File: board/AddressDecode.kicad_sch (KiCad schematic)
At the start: 24 parts, among them U10 74LS260, U11 74F86, U12 74F20, U13 74F30, U14 74F32, U15 74F00, U16 74LS154, U17 74F541, U18 74F138, U19 74F240, U8 74LS260, U9 74F08

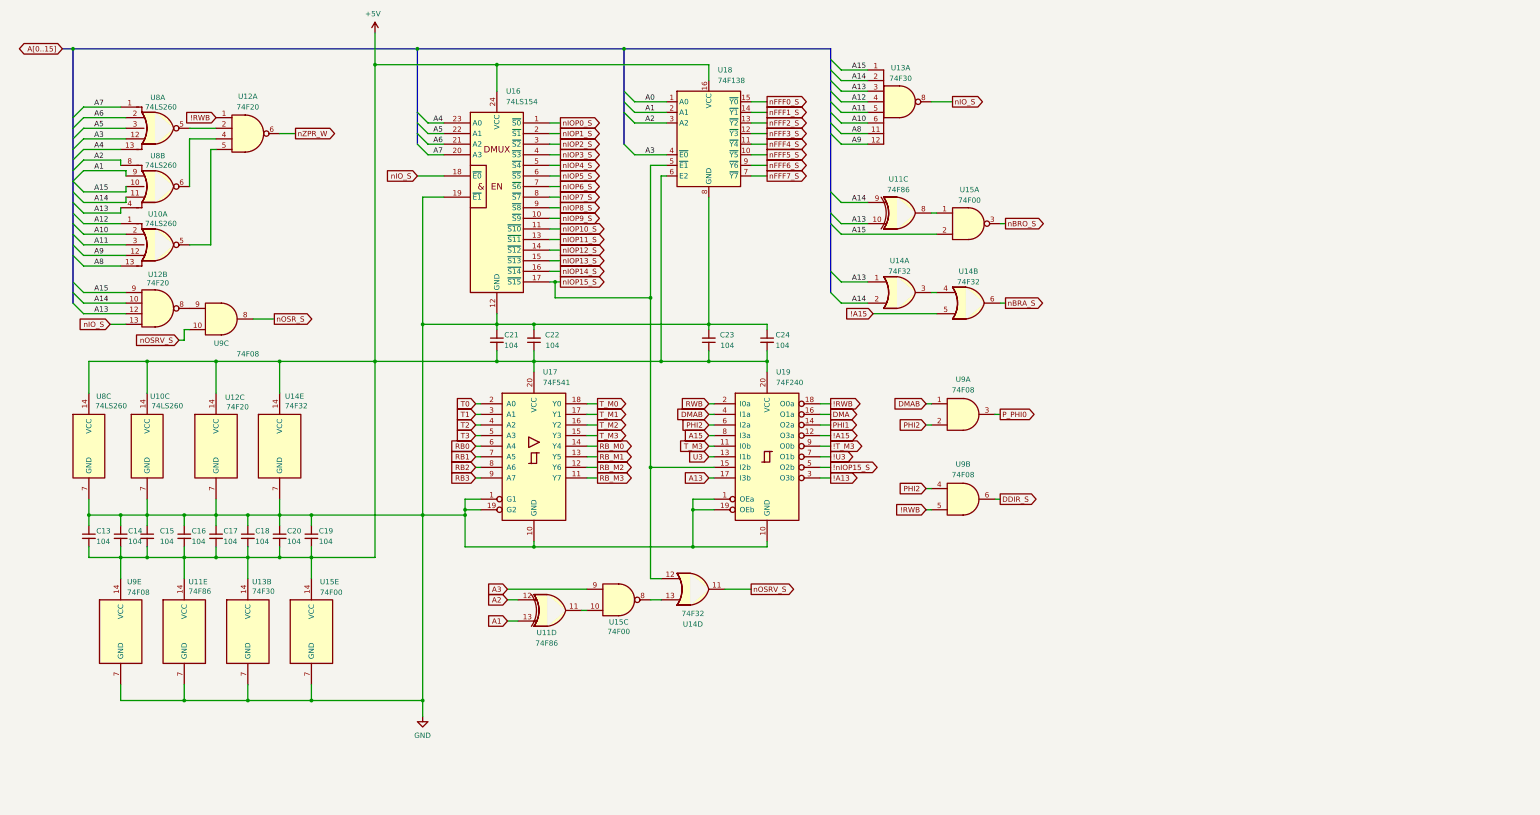
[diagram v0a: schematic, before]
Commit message: V2.0: wait states, GAL glue logic, serial clock and review fixes
Main board schematic:
- Replace the T4-T7 clock divider with RDY wait states. Fixed 7.16 MHz
  CPU clock; J36 selects 3.58 MHz for Rockwell parts. Waits are set per
  region through the write-only register at $FFF5 (reset = 3 waits).
- Move address decode, strobes, the wait-state generator, the IRQ
  encoder/latch/vector mux, ROM bank gating and DMA sync into seven GALs
  (U81-U86 ATF22V10C, U87 ATF16V8C), removing 29 ICs. CUPL sources,
  JEDECs and notes are in board/PLDs/V2.
- 1.8432 MHz serial clock, soft-power latch, -5V regulator, bulk caps,
  pull-ups, audio coupling/decoupling, GNDA tie, read-only Z register
  and other design-review fixes.
- New WaitStates and Support sheets; project symbol library
  hydra16.kicad_sym with sym-lib-table.

PCB updated from the schematic. Includes pending changes to the counter,
bus breakout and memory daughter card projects.

Firmware:
- Remove S_REGISTER; T/U/V/W now at $FFF0-$FFF3 to match the hardware.
- Add math.s and sound.s (included by os_main.s).
- Rebuild the 65C02 ROM image.

Co-Authored-By: Claude Opus 5.5 <noreply@anthropic.com>
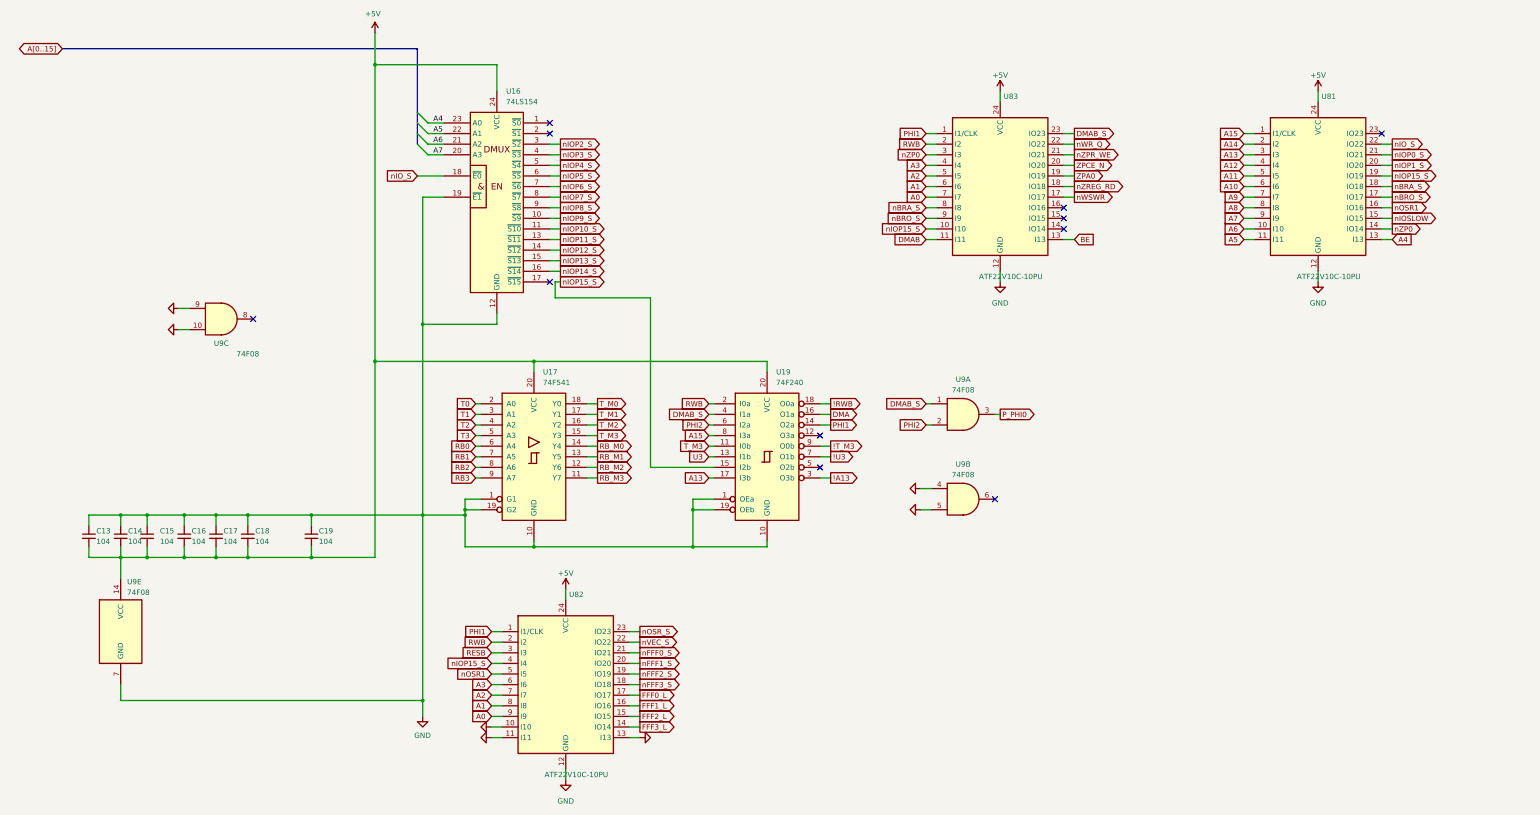
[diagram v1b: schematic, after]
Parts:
- removed C20, C21, C22, C23, C24: 104, Capacitor_THT:C_Disc_D5.0mm_W2.5mm_P5.00mm, symbol Device:C_Small
- removed U10, U8: 74LS260, Package_DIP:DIP-14_W7.62mm_Socket_LongPads, symbol Other_TTL:74LS260
- removed U11: 74F86, Package_DIP:DIP-14_W7.62mm_Socket_LongPads, symbol 74xx:74LS86
- removed U12: 74F20, Package_DIP:DIP-14_W7.62mm_Socket_LongPads, symbol 74xx:74LS20
- removed U13: 74F30, Package_DIP:DIP-14_W7.62mm_Socket_LongPads, symbol 74xx:74LS30
- removed U14: 74F32, Package_DIP:DIP-14_W7.62mm_Socket_LongPads, symbol 74xx:74LS32
- removed U15: 74F00, Package_DIP:DIP-14_W7.62mm_Socket_LongPads, symbol 74xx:74LS00
- removed U18: 74F138, Package_DIP:DIP-16_W7.62mm_Socket_LongPads, symbol 74xx:74HC138
- added U81, U82, U83: ATF22V10C-10PU, Package_DIP:DIP-24_W7.62mm_Socket_LongPads, symbol Hydra16:ATF22V10C
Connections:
- net nOSRV_S is gone; now on net GND: U9.10
- net !RWB: no longer U9.5
- net +5V: now also U81.24 (VCC), U82.24 (VCC), U83.24 (VCC)
- net A0: now also U82.9 (I9), U83.7 (I7)
- net A1: now also U82.8 (I8), U83.6 (I6)
- net A10: now also U81.6 (I6)
- net A11: now also U81.5 (I5)
- net A12: now also U81.4 (I4)
- net A13: now also U81.3 (I3)
- net A14: now also U81.2 (I2)
- net A15: now also U81.1 (I1/CLK)
- net A2: now also U82.7 (I7), U83.5 (I5)
- net A3: now also U82.6 (I6), U83.4 (I4)
- net A4: now also U81.13 (I13)
- net A5: now also U81.11 (I11)
- net A6: now also U81.10 (I10)
- net A7: now also U81.9 (I9)
- net A8: now also U81.8 (I8)
- net A9: now also U81.7 (I7)
- net DMAB: now also U83.11 (I11); no longer U19.4 (I1a), U9.1
- net GND: now also U9.4, U9.5, U9.9, U81.12 (GND), U82.10 (I10), U82.11 (I11), U82.12 (GND), U82.13 (I13), U83.12 (GND)
- net PHI1: now also U82.1 (I1/CLK), U83.1 (I1/CLK)
- net PHI2: no longer U9.4
- net RWB: now also U82.2 (I2), U83.2 (I2)
- net nBRA_S: now also U81.18 (IO18), U83.8 (I8)
- net nBRO_S: now also U81.17 (IO17), U83.9 (I9)
- net nFFF0_S: now also U82.21 (IO21)
- net nFFF1_S: now also U82.20 (IO20)
- net nFFF2_S: now also U82.19 (IO19)
- net nFFF3_S: now also U82.18 (IO18)
- net nIOP0_S: now also U81.21 (IO21); no longer U16.1 (~{S0})
- net nIOP15_S: now also U81.19 (IO19), U82.4 (I4), U83.10 (I10); no longer U16.17 (~{S15})
- net nIOP1_S: now also U81.20 (IO20); no longer U16.2 (~{S1})
- net nIO_S: now also U81.22 (IO22)
- net nOSR_S: now also U82.23 (IO23); no longer U9.8
- net !A15: no longer names the net of U19.12 (O3a)
- net !nIOP15_S: no longer names the net of U19.5 (O2b)
- net DDIR_S: no longer names the net of U9.6
- new net BE: U83.13 (I13)
- new net DMAB_S: U19.4 (I1a), U83.23 (IO23), U9.1
- new net FFF0_L: U82.17 (IO17)
- new net FFF1_L: U82.16 (IO16)
- new net FFF2_L: U82.15 (IO15)
- new net FFF3_L: U82.14 (IO14)
- new net RESB: U82.3 (I3)
- new net ZPA0: U83.19 (IO19)
- new net ZPCE_N: U83.20 (IO20)
- new net nIOSLOW: U81.15 (IO15)
- new net nOSR1: U81.16 (IO16), U82.5 (I5)
- new net nVEC_S: U82.22 (IO22)
- new net nWR_Q: U83.22 (IO22)
- new net nWSWR: U83.17 (IO17)
- new net nZP0: U81.14 (IO14), U83.3 (I3)
- new net nZPR_WE: U83.21 (IO21)
- new net nZREG_RD: U83.18 (IO18)
- no-connect marks 0 -> 11

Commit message: V2.0 rev 2.0D: clock stretching, OS ROM paging and review fixes
Bus timing:
- New GAL C (U88) generates PHI2/PHI1 and the 3.58 MHz sound clock from
  the 14.318 MHz master, replacing the U35 74F191 divider. J36 now selects
  7.16 or 3.58 MHz.
- Banked RAM, banked ROM and slot I/O ($FF20-$FFEF) get one extra PHI2-low
  period plus 0-3 extra PHI2-high periods set in $FFF5 (GAL D). This
  replaces the on-board RDY wait generator; cards can still pull RDY.
- Write strobes are now hold-time safe: PHI1 comes straight from GAL C
  and RWB_M straight from GAL B2.

Review fixes:
- OS ROM chip enable from a single-level decode, output enable from
  GAL B1; -55 part specified. Full 4K OS ROM paging via GAL G.
- Vector RAM writes only during PHI2; $FFF0-$FFFF no longer slowed.
- YM2151 /WR on RWB_M. U62 removed. RB0-RB7 pull-ups (RN5).
- Slot clocks driven through U56 and U34 with 33R series resistors.
- J38 enables in-system flashing of the banked ROMs.
- W65C22S/W65C51N, AS6C4008, DS1813-5 and CY7C192-25 values; R4 1k.
- J7 pin 8 no longer +5V; +5VA renamed +5VSB; serial handshake loop.
- Sheet titles and revisions, slot symbol pin fixes, and project symbol
  and footprint libraries so the project opens on another machine.

Co-Authored-By: Claude Opus 5.5 <noreply@anthropic.com>
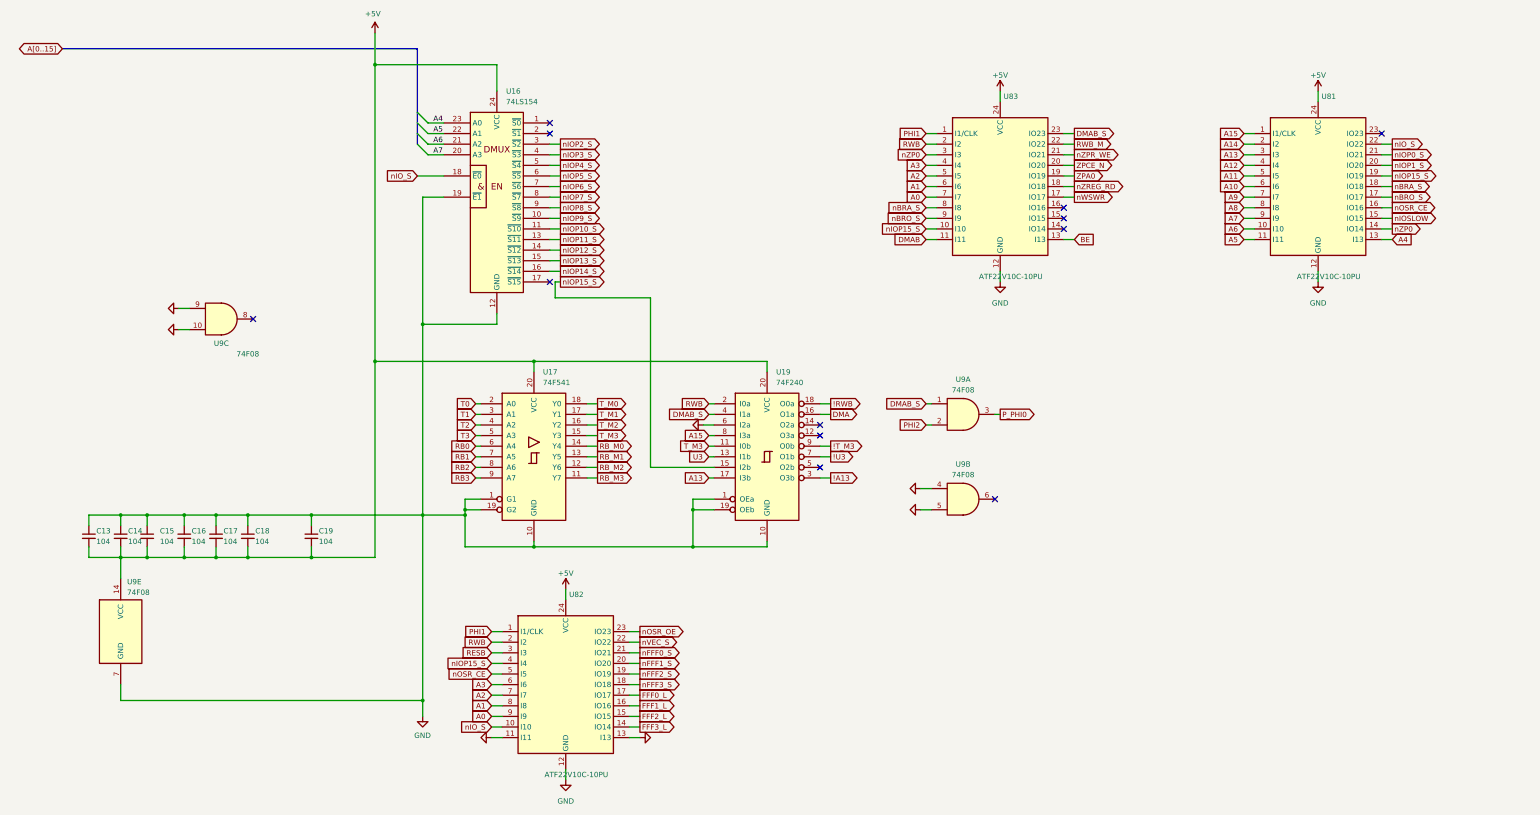
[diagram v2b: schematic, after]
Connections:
- net GND: now also U19.6 (I2a); no longer U82.10 (I10)
- net PHI1: no longer U19.14 (O2a)
- net PHI2: no longer U19.6 (I2a)
- net nIO_S: now also U82.10 (I10)
- net nOSR1 renamed nOSR_CE
- net nOSR_S renamed nOSR_OE
- net nWR_Q renamed RWB_M
- no-connect marks 11 -> 12
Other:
- title: ZeroPage $00/$01 Mirror Memory and RAM/ROM Bank Logic -> Address Decode and Bus Strobes (GALs)
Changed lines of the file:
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@@
 	(paper "USLedger")
 	(title_block
-		(title "ZeroPage $00/$01 Mirror Memory and RAM/ROM Bank Logic")
-		(date "2026-01-28")
-		(rev "2.0B")
+		(title "Address Decode and Bus Strobes (GALs)")
+		(date "2026-10-06")
+		(rev "2.0D")
 		(company "Data Tuning")
 		(comment 1 "Hydra 16")
@@
 		(at 269.24 66.04)
 	)
+	(no_connect
+		(at 210.82 118.11)
+	)
 	(bus_entry
 		(at 114.3 48.26)
@@
 	(wire
 		(pts
-			(xy 134.62 190.5) (xy 132.08 190.5)
-		)
-		(stroke
-			(width 0)
-			(type default)
-		)
-	)
-	(wire
-		(pts
 			(xy 104.14 24.13) (xy 104.14 31.75)
 		)
@@
 	(wire
 		(pts
-			(xy 213.36 118.11) (xy 210.82 118.11)
-		)
-		(stroke
-			(width 0)
-			(type default)
-		)
-	)
-	(wire
-		(pts
 			(xy 43.18 149.86) (xy 43.18 154.94)
 		)
@@
 	(wire
 		(pts
-			(xy 184.15 118.11) (xy 185.42 118.11)
-		)
-		(stroke
-			(width 0)
-			(type default)
-		)
-	)
-	(wire
-		(pts
 			(xy 269.24 58.42) (xy 271.78 58.42)
 		)
@@
 		)
 	)
+	(wire
+		(pts
+			(xy 185.42 118.11) (xy 182.88 118.11)
+		)
+		(stroke
+			(width 0)
+			(type default)
+		)
+	)
+	(wire
+		(pts
+			(xy 134.62 190.5) (xy 132.08 190.5)
+		)
+		(stroke
+			(width 0)
+			(type default)
+		)
+	)
 	(label "A6"
 		(at 118.11 50.8 0)
@@
 		)
 	)
-	(global_label "nOSR_S"
+	(global_label "nOSR_OE"
 		(shape output)
 		(at 167.64 167.64 0)
@@
 		)
 	)
-	(global_label "nWR_Q"
+	(global_label "RWB_M"
 		(shape output)
 		(at 271.78 50.8 0)
@@
 		)
 	)
-	(global_label "nOSR1"
+	(global_label "nOSR_CE"
 		(shape input)
 		(at 132.08 177.8 180)
@@
 		)
 	)
-	(global_label "nOSR1"
+	(global_label "nOSR_CE"
 		(shape output)
 		(at 347.98 66.04 0)
@@
 		)
 	)
-	(global_label "PHI2"
-		(shape input)
-		(at 184.15 118.11 180)
-		(fields_autoplaced yes)
-		(effects
-			(font
-				(size 1.27 1.27)
-			)
-			(justify right)
-		)
-		(property "Intersheetrefs" "${INTERSHEET_REFS}"
-			(at 176.75 118.11 0)
-			(effects
-				(font
-					(size 1.27 1.27)
-				)
-				(justify right)
-				(hide yes)
-			)
-		)
-	)
 	(global_label "P_PHI0"
 		(shape output)
@@
 		)
 	)
-	(global_label "PHI1"
+	(global_label "nZP0"
 		(shape output)
-		(at 213.36 118.11 0)
+		(at 347.98 71.12 0)
 		(fields_autoplaced yes)
 		(effects
@@
 		)
 		(property "Intersheetrefs" "${INTERSHEET_REFS}"
-			(at 221.3648 118.11 0)
+			(at 347.98 71.12 0)
 			(effects
 				(font
@@
 		)
 	)
-	(global_label "nZP0"
-		(shape output)
-		(at 347.98 71.12 0)
+	(global_label "nBRO_S"
+		(shape input)
+		(at 236.22 68.58 180)
 		(fields_autoplaced yes)
 		(effects
@@
 				(size 1.27 1.27)
 			)
-			(justify left)
+			(justify right)
 		)
 		(property "Intersheetrefs" "${INTERSHEET_REFS}"
-			(at 347.98 71.12 0)
+			(at 236.22 68.58 180)
 			(effects
 				(font
 					(size 1.27 1.27)
 				)
-				(justify left)
+				(justify right)
 				(hide yes)
 			)
 		)
 	)
-	(global_label "nBRO_S"
+	(global_label "nIO_S"
 		(shape input)
-		(at 236.22 68.58 180)
+		(at 132.08 190.5 180)
 		(fields_autoplaced yes)
 		(effects
@@
 		)
 		(property "Intersheetrefs" "${INTERSHEET_REFS}"
-			(at 236.22 68.58 180)
+			(at 132.08 190.5 180)
 			(effects
 				(font
@@
 	)
 	(symbol
-		(lib_id "power:GND")
-		(at 132.08 190.5 270)
-		(unit 1)
-		(exclude_from_sim no)
-		(in_bom yes)
-		(on_board yes)
-		(dnp no)
-		(property "Reference" "#PWR229"
-			(at 132.08 190.5 0)
-			(effects
-				(font
-					(size 1.27 1.27)
-				)
-				(hide yes)
-			)
-		)
-		(property "Value" "GND"
-			(at 127 190.5 0)
-			(effects
-				(font
-					(size 1.27 1.27)
-				)
-				(hide yes)
-			)
-		)
-		(property "Footprint" ""
-			(at 132.08 190.5 0)
-			(effects
-				(font
-					(size 1.27 1.27)
-				)
-				(hide yes)
-			)
-		)
-		(property "Datasheet" ""
-			(at 132.08 190.5 0)
-			(effects
-				(font
-					(size 1.27 1.27)
-				)
-				(hide yes)
-			)
-		)
-		(property "Description" "Power symbol creates a global label with name \"GND\""
-			(at 132.08 190.5 0)
-			(effects
-				(font
-					(size 1.27 1.27)
-				)
-				(hide yes)
-			)
-		)
-		(pin "1"
-		)
-		(instances
-			(project "hydra-16"
-				(path "/ef29fc71-3fec-48b5-8a1a-46bee537a98c/e447d2ea-fe27-4cfd-bb5f-eaf105a9519f"
-					(reference "#PWR229")
-					(unit 1)
-				)
-			)
-		)
-	)
-	(symbol
 		(lib_id "Device:C_Small")
 		(at 73.66 144.78 0)
@@
 					(unit 1)
 				)
+			)
+		)
+	)
+	(symbol
+		(lib_id "power:GND")
+		(at 182.88 118.11 270)
+		(unit 1)
+		(exclude_from_sim no)
+		(in_bom yes)
+		(on_board yes)
+		(dnp no)
+		(property "Reference" "#PWR2248"
+			(at 182.88 118.11 0)
+			(effects
+				(font
+					(size 1.27 1.27)
+				)
+				(hide yes)
+			)
+		)
+		(property "Value" "GND"
+			(at 177.8 118.11 0)
+			(effects
+				(font
+					(size 1.27 1.27)
+				)
+				(hide yes)
+			)
+		)
+		(property "Footprint" ""
+			(at 182.88 118.11 0)
+			(effects
+				(font
+					(size 1.27 1.27)
+				)
+				(hide yes)
+			)
+		)
+		(property "Datasheet" ""
+			(at 182.88 118.11 0)
+			(effects
+				(font
+					(size 1.27 1.27)
+				)
+				(hide yes)
+			)
+		)
+		(property "Description" "Power symbol creates a global label with name \"GND\""
+			(at 182.88 118.11 0)
+			(effects
+				(font
+					(size 1.27 1.27)
+				)
+				(hide yes)
+			)
+		)
+		(pin "1"
+		)
+		(instances
+			(project "hydra-16"
+				(path "/ef29fc71-3fec-48b5-8a1a-46bee537a98c/e447d2ea-fe27-4cfd-bb5f-eaf105a9519f"
+					(reference "#PWR2248")
+					(unit 1)
+				)
